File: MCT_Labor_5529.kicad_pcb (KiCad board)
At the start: 2 copper layers, 160 x 100 mm, 143 parts, among them J1 Micro_SD_Card_Det, J10 Conn_01x04_Male, J11 Conn_01x01_Female, J12 Conn_01x01_Female, J13 Conn_01x01_Female, J14 Conn_02x05_Odd_Even, J18 Screw_Terminal_01x02, J2 Conn_02x05_Odd_Even, J3 Grove, J4 Conn_02x04_Odd_Even, J5 Grove, J6 Grove, J7 Conn_01x04_Male, J8 Conn_01x01_Female, Q1 BSS138, SW1 SW_Push, SW2 SW_Push, SW3 SW_SPDT, U1 RC1602A, U10 msp-exp430f5529-LP, U11 MCP73831, U12 TPS73733, U2 ULN2003, U3 74148, U4 74_138, U5 NRF24L01_Breakout, U6 74HCT595, U7 ESP-12E, U8 LM75B, U9 STC3100, X1 XBee_S3

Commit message: Alle Bauteile platziert
Alle Bauteile sind grob plaziert.
Einige Bauteile sollten noch umplaziert werden (u. a. die Jumper links neben Groov-Con, RGB-LED,).
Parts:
- moved R38 458.8 mm to (75.7, 122.0), turned to 180 degrees
- moved R28 420.2 mm to (106.9, 107.9), turned to 90 degrees
- moved C4 417.0 mm to (90.1, 67.1)
- moved R29 411.2 mm to (109.6, 93.3)
- moved C3 408.6 mm to (115.4, 72.6), turned to 270 degrees
- moved R17 406.1 mm to (96.9, 62.4), turned to 270 degrees
- moved D11 398.3 mm to (130.5, 123.9)
- moved R33 397.8 mm to (130.4, 119.6), turned to 180 degrees
- moved C6 395.3 mm to (111.8, 121.1), turned to 270 degrees
- moved D10 393.0 mm to (106.8, 99.1), turned to 270 degrees
- moved R30 392.7 mm to (109.6, 95.0)
- moved C9 384.7 mm to (110.1, 87.9)
- moved R37 381.2 mm to (79.1, 118.3), turned to 270 degrees
- moved U9 381.0 mm to (76.4, 117.5), turned to 270 degrees
- moved C15 378.9 mm to (80.9, 118.3), turned to 90 degrees
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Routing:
- net GND: track 0.00 -> 63.7 mm, vias 0 -> 22
- net +5V: track 0.00 -> 45.6 mm, vias 0 -> 1
- net Net-(J1-Pad11): track 0.00 -> 32.6 mm
- net Net-(RV1-Pad2): track 0.00 -> 22.0 mm
- net Net-(RN1-Pad9): track 0.00 -> 12.5 mm
- net Net-(RN1-Pad6): track 0.00 -> 12.5 mm
- net Net-(RN1-Pad5): track 0.00 -> 12.5 mm
- net Net-(RN1-Pad4): track 0.00 -> 12.5 mm
- net Net-(RN1-Pad3): track 0.00 -> 12.5 mm
- net +3V3: track 0.00 -> 3.31 mm
- net Net-(LD_F2-Pad2): track 0.00 -> 3.13 mm
- net Net-(LD_F1-Pad2): track 0.00 -> 2.39 mm
- net Net-(LD_F3-Pad2): track 0.00 -> 2.32 mm
- net Net-(R33-Pad1): track 0.00 -> 0.75 mm
- added copper zone on F.Cu, net +3V3
- added copper zone on B.Cu, net GND

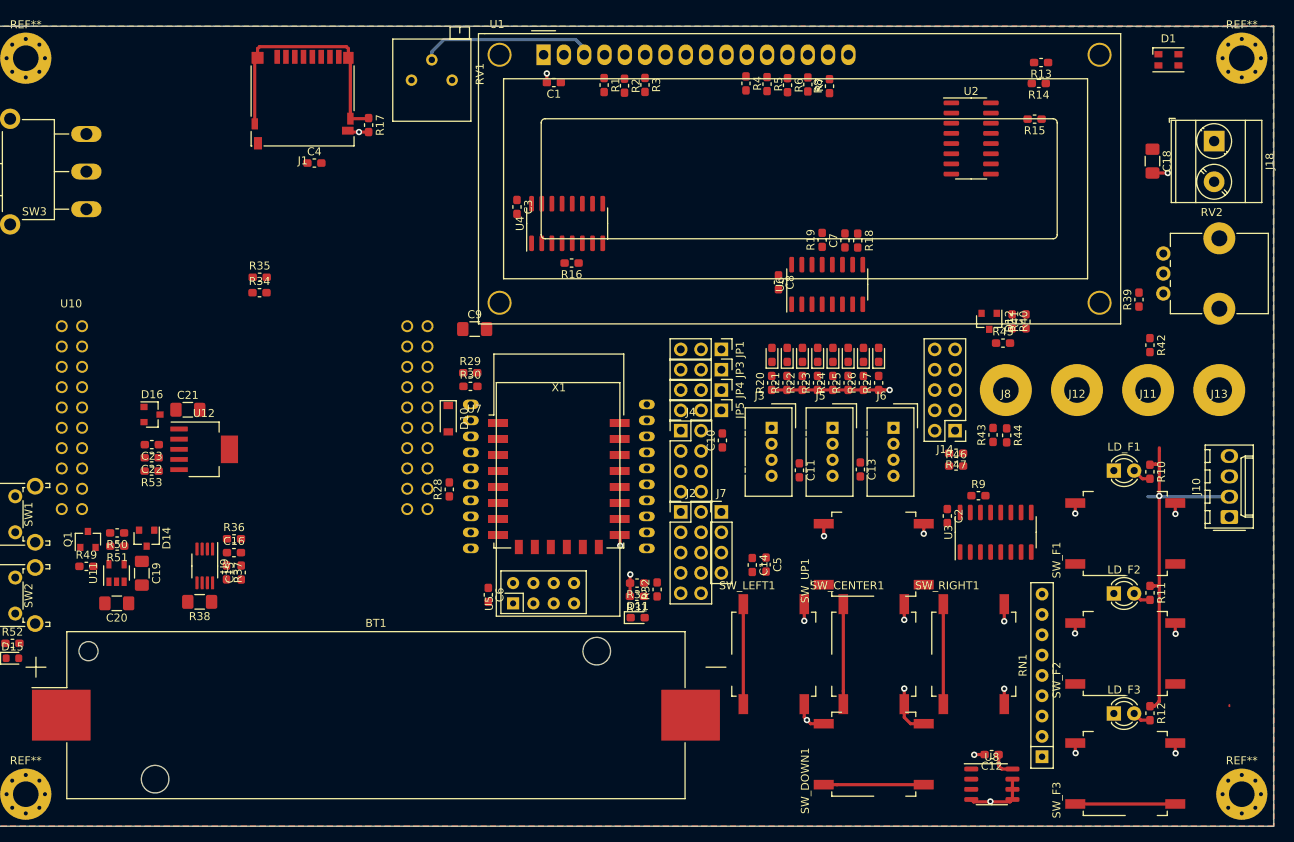
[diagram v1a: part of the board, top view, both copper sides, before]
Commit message: Routing der rechten Platinenhälfte
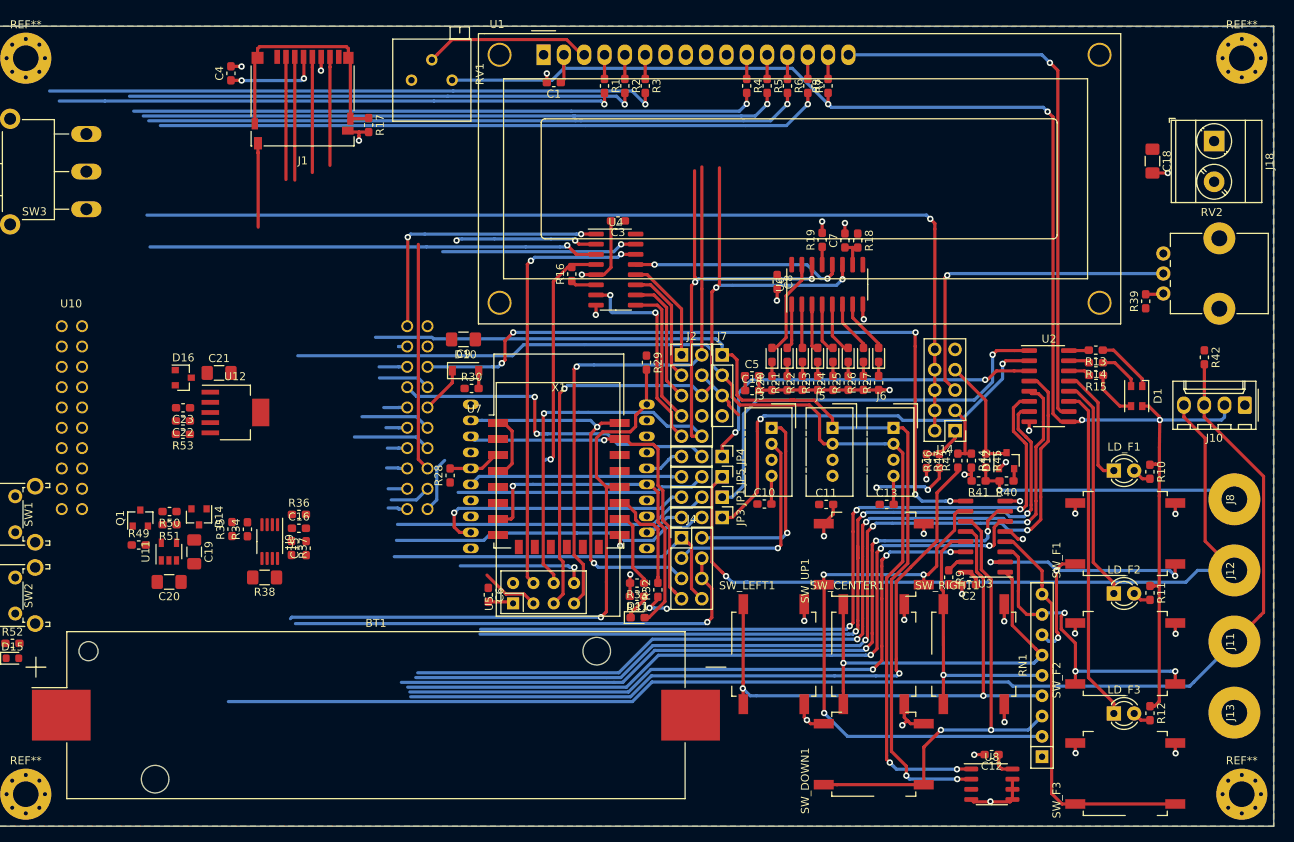
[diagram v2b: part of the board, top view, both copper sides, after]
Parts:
- moved D1 42.2 mm to (192.9, 96.2), turned to 270 degrees
- moved J13 40.4 mm to (205.1, 135.8), turned to 270 degrees
- moved R13 36.6 mm to (187.8, 90.5)
- moved R14 35.6 mm to (187.8, 92.1)
- moved J11 33.2 mm to (205.1, 126.9), turned to 270 degrees
- moved R15 32.9 mm to (187.8, 93.6)
- moved U2 32.5 mm to (181.9, 95.0)
- moved R35 31.7 mm to (79.8, 112.9), turned to 90 degrees
- moved J8 31.7 mm to (205.1, 109.1), turned to 270 degrees
- moved J12 29.9 mm to (205.1, 118.0), turned to 270 degrees
- moved R34 29.6 mm to (81.7, 112.9), turned to 90 degrees
- moved C5 23.7 mm to (144.8, 93.7), turned to 0 degrees
- moved R29 22.1 mm to (131.6, 92.1), turned to 270 degrees
- moved C14 21.8 mm to (144.8, 95.5), turned to 0 degrees
- moved R41 20.8 mm to (173.1, 106.8), turned to 180 degrees
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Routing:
- net /Launchpad/P1.6: track 0.00 -> 168.5 mm
- net +5V: track 45.6 -> 187.6 mm, vias 1 -> 4
- net /Launchpad/P4.1: track 0.00 -> 135.8 mm, vias 0 -> 2
- net /Launchpad/P4.2: track 0.00 -> 128.8 mm, vias 0 -> 2
- net /Launchpad/P7.0: track 0.00 -> 124.9 mm, vias 0 -> 1
- net /SPI/MOSI: track 0.00 -> 118.2 mm, vias 0 -> 3
- net /LED-Treiber/LED_4: track 0.00 -> 114.1 mm, vias 0 -> 3
- net /LED-Treiber/LED_5: track 0.00 -> 110.8 mm, vias 0 -> 3
- net /Launchpad/P3.2: track 0.00 -> 107.5 mm, vias 0 -> 3
- net /LED-Treiber/LED_7: track 0.00 -> 101.8 mm, vias 0 -> 3
- net /Launchpad/P1.5_FAN: track 0.00 -> 101.7 mm, vias 0 -> 1
- net /LED-Treiber/LED_6: track 0.00 -> 100.4 mm, vias 0 -> 3
- net /Button_decoder/BTN_S1: track 0.00 -> 98.6 mm, vias 0 -> 3
- net /SPI/MISO: track 0.00 -> 93.7 mm, vias 0 -> 1
- net /Button_decoder/BTN_S2: track 0.00 -> 92.8 mm, vias 0 -> 3
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
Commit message: Routing komplett
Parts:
- moved D16 9.67 mm to (74.7, 103.6), turned to 180 degrees
- moved R53 8.48 mm to (81.7, 103.5), turned to 270 degrees
- moved R34 7.85 mm to (86.3, 106.5), turned to 270 degrees
- moved R51 7.69 mm to (68.2, 119.0)
- moved C22 7.67 mm to (80.1, 103.5), turned to 270 degrees
- moved C23 7.53 mm to (78.4, 103.5), turned to 270 degrees
- moved R50 7.45 mm to (70.8, 118.0), turned to 90 degrees
- moved R35 7.17 mm to (83.2, 106.6), turned to 270 degrees
- moved C21 7.01 mm to (74.1, 99.0), turned to 90 degrees
- moved R30 5.37 mm to (108.8, 90.0)
- moved Q1 4.77 mm to (68.1, 116.2), turned to 270 degrees
- moved C9 3.31 mm to (108.6, 85.8), turned to 90 degrees
- moved C20 3.15 mm to (74.2, 121.6)
- moved U11 2.78 mm to (73.6, 117.9)
- moved D14 2.67 mm to (75.4, 108.7)
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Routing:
- net /Launchpad/P3.2: track 107.5 -> 231.1 mm, vias 3 -> 11
- net VDD: track 0.00 -> 109.0 mm, vias 0 -> 15
- net /SPI/MOSI: track 118.2 -> 211.7 mm, vias 3 -> 8
- net +BATT: track 91.4 -> 176.2 mm, vias 1 -> 12
- net /SPI/MISO: track 93.7 -> 167.9 mm, vias 1 -> 6
- net Net-(BT1-Pad2): track 0.00 -> 69.4 mm
- net /Launchpad/P4.2: track 128.8 -> 194.6 mm, vias 2 -> 5
- net /LED-Treiber/LED_4: track 114.1 -> 177.2 mm, vias 3 -> 4
- net /Launchpad/P3.4: track 60.3 -> 123.0 mm, vias 1 -> 3
- net /LED-Treiber/LED_5: track 110.8 -> 173.5 mm, vias 3 -> 5
- net /Launchpad/P3.3: track 45.7 -> 106.4 mm, vias 0 -> 4
- net Net-(R28-Pad2): track 6.69 -> 65.5 mm
- net /Launchpad/P4.1: track 135.8 -> 192.0 mm, vias 2 -> 4
- net /Button_decoder/BTN_S2: track 92.8 -> 147.1 mm, vias 3 -> 5
- net Net-(C21-Pad1): track 0.00 -> 52.0 mm, vias 0 -> 2
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- added copper zone on B.Cu, net +BATT
- added copper zone on F.Cu, net +BATT
- added copper zone on F.Cu, net GND
- added copper zone on B.Cu, net VDD
- added copper zone on F.Cu, net VDD
